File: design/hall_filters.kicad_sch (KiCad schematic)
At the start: 11 parts

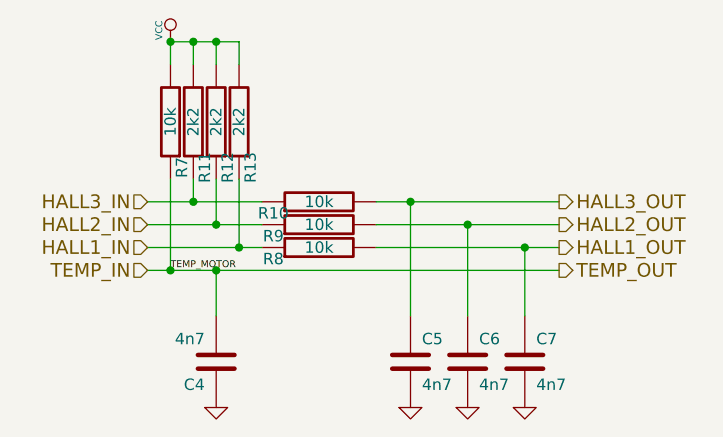
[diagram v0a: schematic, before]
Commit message: v 4.13 produced by jlcpcb
Some serious issues with usb connectors facing the caps. Working fine
otherwise
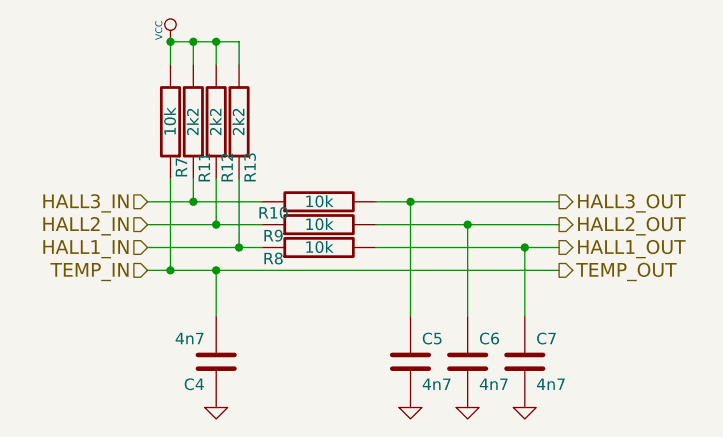
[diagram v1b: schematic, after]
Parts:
- C4, C5, C6, C7: JLCPCB (none) -> C53987
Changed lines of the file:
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@@
 (kicad_sch
-	(version 20231120)
+	(version 20250114)
 	(generator "eeschema")
-	(generator_version "8.0")
+	(generator_version "9.0")
 	(paper "A4")
 	(title_block
 		(title "BLDC Driver 4.11")
 		(date "21 aug 2015")
-		(rev "4.12")
+		(rev "${version}")
 		(company "Benjamin Vedder")
 	)
@@
 		)
 	)
-	(label "TEMP_MOTOR"
-		(at 124.46 97.79 0)
-		(fields_autoplaced yes)
-		(effects
-			(font
-				(size 0.762 0.762)
-			)
-			(justify left bottom)
-		)
-	)
 	(hierarchical_label "HALL3_OUT"
 		(shape output)
 		(at 167.64 90.17 0)
-		(fields_autoplaced yes)
 		(effects
 			(font
@@
 		(shape input)
 		(at 121.92 95.25 180)
-		(fields_autoplaced yes)
 		(effects
 			(font
@@
 		(shape output)
 		(at 167.64 92.71 0)
-		(fields_autoplaced yes)
 		(effects
 			(font
@@
 		(shape input)
 		(at 121.92 90.17 180)
-		(fields_autoplaced yes)
 		(effects
 			(font
@@
 		(shape output)
 		(at 167.64 97.79 0)
-		(fields_autoplaced yes)
 		(effects
 			(font
@@
 		(shape input)
 		(at 121.92 97.79 180)
-		(fields_autoplaced yes)
 		(effects
 			(font
@@
 		(shape output)
 		(at 167.64 95.25 0)
-		(fields_autoplaced yes)
 		(effects
 			(font
@@
 		(shape input)
 		(at 121.92 92.71 180)
-		(fields_autoplaced yes)
 		(effects
 			(font
@@
 			)
 		)
+		(property "JLCPCB" "C53987"
+			(at 151.13 107.95 0)
+			(effects
+				(font
+					(size 1.27 1.27)
+				)
+				(hide yes)
+			)
+		)
 		(pin "1"
 		)
@@
 			)
 		)
+		(property "JLCPCB" "C53987"
+			(at 157.48 107.95 0)
+			(effects
+				(font
+					(size 1.27 1.27)
+				)
+				(hide yes)
+			)
+		)
 		(pin "1"
 		)
@@
 			)
 		)
+		(property "JLCPCB" "C53987"
+			(at 163.83 107.95 0)
+			(effects
+				(font
+					(size 1.27 1.27)
+				)
+				(hide yes)
+			)
+		)
 		(pin "1"
 		)
@@
 			(at 129.54 107.95 0)
 			(effects
+				(font
+					(size 1.27 1.27)
+				)
+				(hide yes)
+			)
+		)
+		(property "JLCPCB" "C53987"
+			(at 129.54 107.95 0)
+			(effects
